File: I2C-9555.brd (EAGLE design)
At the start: 99.4 x 80.6 mm, 80 parts, among them IC1 PCA9555D, J1 I2CRA, J10 DCJ0202-RA, J2 I2CRA, J5 GROVE-4P-2.0-3470130P1, J8 GROVE-4P-2.0-3470130P1, Q0 MOSFET-P-044021001, Q1 MOSFET-P-044021001, Q10 MOSFET-P-044021001, Q11 MOSFET-P-044021001, Q12 MOSFET-P-044021001, Q13 MOSFET-P-044021001, Q14 MOSFET-P-044021001, Q15 MOSFET-P-044021001, Q2 MOSFET-P-044021001, Q3 MOSFET-P-044021001, Q4 MOSFET-P-044021001, Q5 MOSFET-P-044021001, Q6 MOSFET-P-044021001, Q7 MOSFET-P-044021001, Q8 MOSFET-P-044021001, Q9 MOSFET-P-044021001

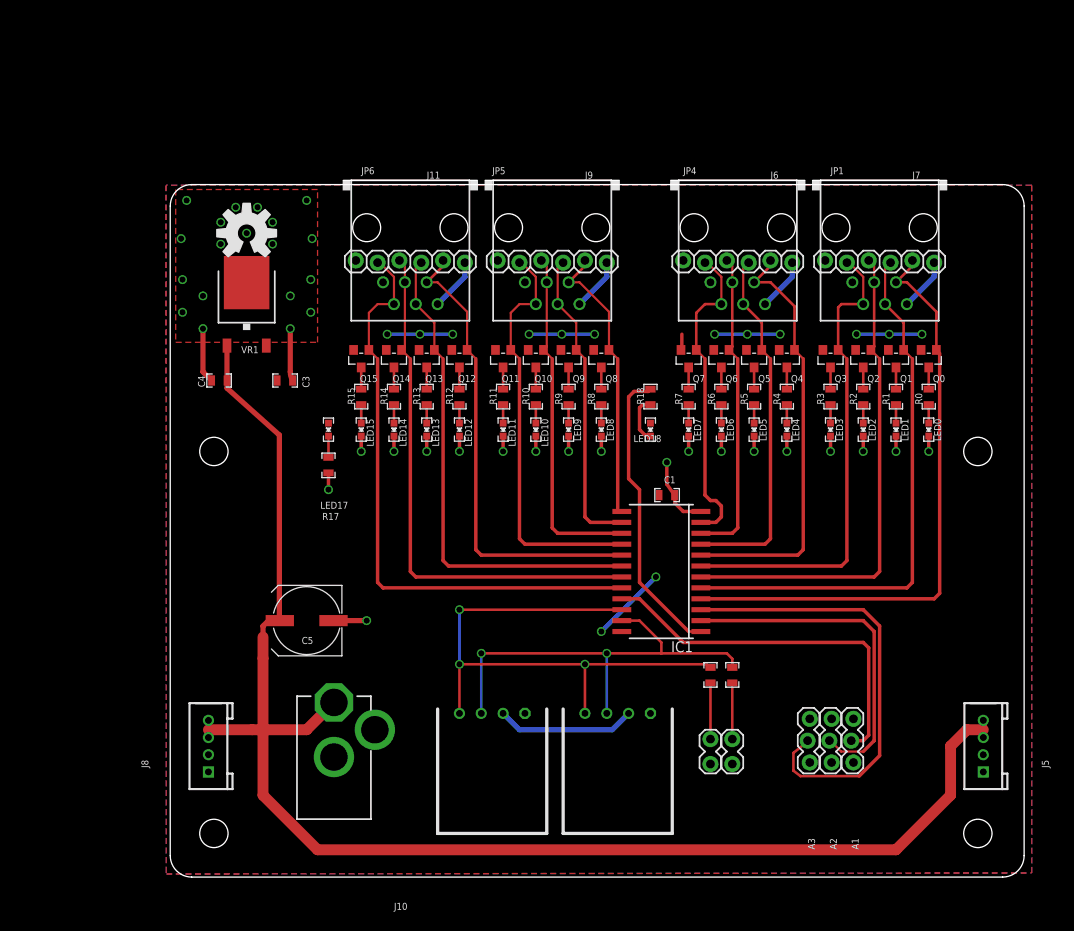
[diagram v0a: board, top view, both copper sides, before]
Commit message: new IOB and power connectors
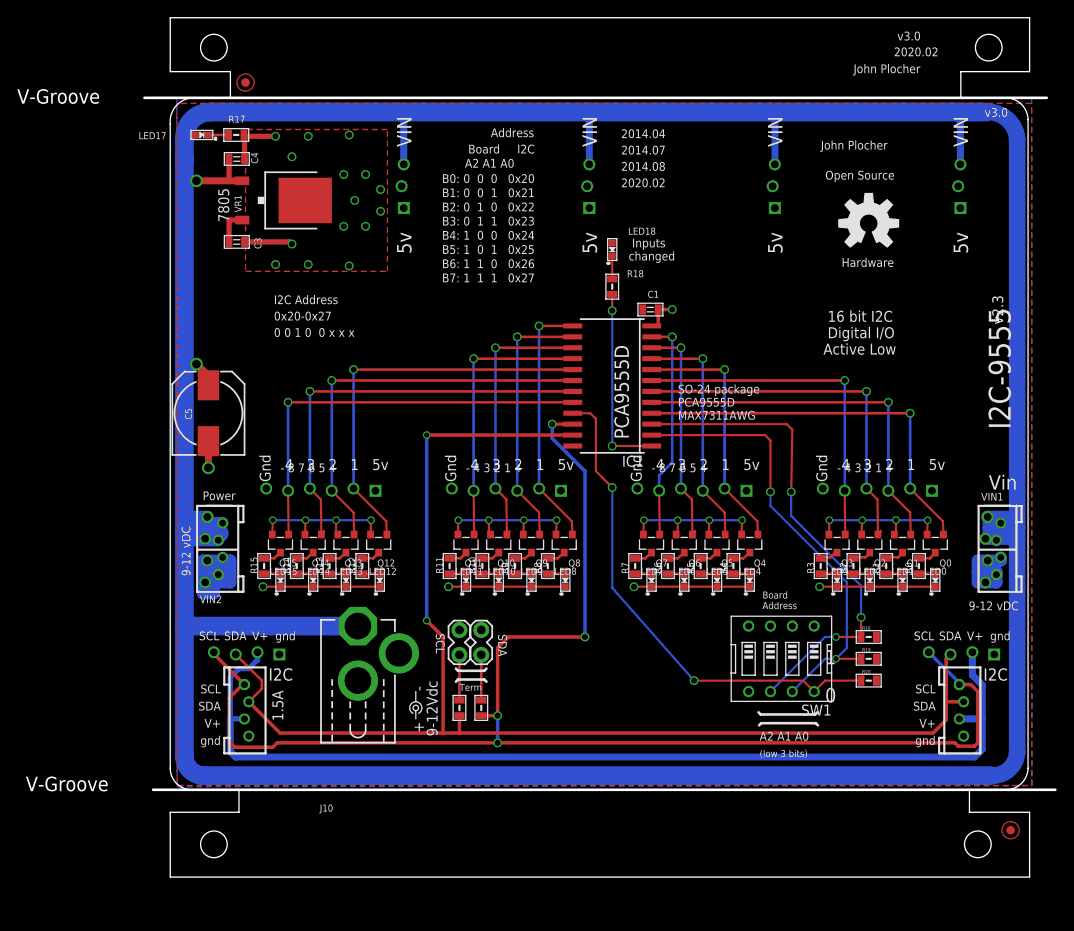
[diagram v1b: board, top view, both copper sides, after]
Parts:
- removed A1, A2, A3: (no value), SparkFun-Connectors:1X03_LOCK
- removed J11, J6, J7, J9: (no value), SPCoast:RJ11-NO_SHIELD
- removed J5, J8: GROVE-4P-2.0-3470130P1, OPL:4P-2.0
- removed JP1, JP4, JP5, JP6: (no value), SparkFun-Connectors:1X06_LOCK
- added BOARD1: BOARD80X100-IOB, SPCoast:BOARD-DINRAIL-3.17IN-IOB
- added FID1, FID2: FIDUCIAL, SPCoast:FIDUCIAL_1MM
- added R16, R19, R20: 10K, SPCoast:0805-RES
- added SW1: (no value), SPCoast:EDG-04
- added U$2, U$3, U$4, U$5: CONNECTOR-IO4-IOBBARE, SPCoast:IO4-IOB
- added VIN1: CONNECTOR-POWER-L, SPCoast:POWER-R2
- added VIN2: CONNECTOR-POWER-R, SPCoast:POWER-R
- C5: device rcl:UD-8X10_NICHICON -> SPCoast:0810-CAP
- J1, J2: value I2CRA -> (none); device SPCoast:I2C -> SPCoast:I2C-L
- J10: value DCJ0202-RA -> (none)
- LED17, LED18: value G - 0330010P1 -> G
- POWER: device SPCoast:POWER_USAGE -> SPCoast:PWR_LABEL
- Q0, Q1, Q10, Q11, Q12, Q13, Q14, Q15, Q2, Q3, Q4, Q5, Q6, Q7, Q8, Q9: value MOSFET-P-044021001 -> (none); device OPL:SOT23 -> SPCoast:SOT23-3
- moved U$1 72.4 mm to (81.3, 76.1)
- moved J1 40.6 mm to (92.1, 26.0)
- moved R17 39.9 mm to (7.68, 86.4), turned to 0 degrees
- moved LED17 37.3 mm to (3.68, 86.4), turned to 0 degrees
- moved SCL 33.3 mm to (33.7, 26.0), turned to 90 degrees
- moved R23 32.0 mm to (33.7, 19.7), turned to 270 degrees
- moved J2 29.4 mm to (8.89, 26.0)
- moved SDA 28.5 mm to (36.2, 26.0), turned to 90 degrees
- moved R22 26.9 mm to (36.2, 19.7), turned to 270 degrees
- moved C5 26.7 mm to (4.45, 54.0), turned to 90 degrees
- moved C4 25.9 mm to (7.75, 83.6), turned to 0 degrees
- moved Q12 23.4 mm to (24.3, 38.9)
- moved Q13 23.4 mm to (20.4, 38.9)
- moved Q14 23.4 mm to (16.6, 38.9)
- moved Q15 23.4 mm to (12.8, 38.9)
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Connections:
- net +9V: now also U$2.V+, U$3.V+, U$4.V+, U$5.V+, VIN1.V+, VIN1.V+@1, VIN1.V+@2, VIN1.V+@3, VIN2.V+, VIN2.V+@1, VIN2.V+@2, VIN2.V+@3; no longer J5.3, J5.4, J8.3, J8.4
- net A0: now also R20.1, SW1.8; no longer A1.2
- net A1: now also R19.1, SW1.7; no longer A2.2
- net A2: now also R16.1, SW1.6; no longer A3.2
- net GND: now also J1.GND@1, J2.GND@1, SW1.1, SW1.2, SW1.3, U$2.G@3, U$3.G@3, U$4.G@3, U$5.G@3, VIN1.GND, VIN1.GND@1, VIN1.GND@2, VIN1.GND@3, VIN2.GND, VIN2.GND@1, VIN2.GND@2, VIN2.GND@3; no longer A1.3, A2.3, A3.3, J11.6, J5.1, J5.2, J6.6, J7.6, J8.1, J8.2, J9.6, JP1.1, JP4.1, JP5.1, JP6.1
- net N$39: now also J1.V+@1, J2.V+@1
- net P1: now also U$2.P1; no longer J7.2, JP1.5
- net P10: now also U$4.P2; no longer J9.3, JP5.4
- net P11: now also U$4.P3; no longer J9.4, JP5.3
- net P12: now also U$4.P4; no longer J9.5, JP5.2
- net P13: now also U$5.P1; no longer J11.2, JP6.5
- net P14: now also U$5.P2; no longer J11.3, JP6.4
- net P15: now also U$5.P3; no longer J11.4, JP6.3
- net P16: now also U$5.P4; no longer J11.5, JP6.2
- net P2: now also U$2.P2; no longer J7.3, JP1.4
- net P3: now also U$2.P3; no longer J7.4, JP1.3
- net P4: now also U$2.P4; no longer J7.5, JP1.2
- net P5: now also U$3.P1; no longer J6.2, JP4.5
- net P6: now also U$3.P2; no longer J6.3, JP4.4
- net P7: now also U$3.P3; no longer J6.4, JP4.3
- net P8: now also U$3.P4; no longer J6.5, JP4.2
- net P9: now also U$4.P1; no longer J9.2, JP5.5
- net SCL: now also J1.SCL@1, J2.SCL@1
- net SDA: now also J1.SDA@1, J2.SDA@1
- net VCC: now also R16.2, R19.2, R20.2, U$2.V5, U$2.V5@1, U$3.V5, U$3.V5@1, U$4.V5, U$4.V5@1, U$5.V5, U$5.V5@1; no longer A1.1, A2.1, A3.1, J11.1, J6.1, J7.1, J9.1, JP1.6, JP4.6, JP5.6, JP6.6
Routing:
- net +9V: track 173.3 -> 439.1 mm, vias 0 -> 2
- net SDA: track 51.4 -> 155.0 mm
- net N$39: track 16.2 -> 117.8 mm
- net SCL: track 66.0 -> 166.7 mm, vias 3 -> 4
- net GND: track 55.4 -> 102.6 mm, vias 38 -> 21
- net P1: track 70.4 -> 45.8 mm, vias 0 -> 1
- net P16: track 69.6 -> 48.5 mm, vias 0 -> 1
- net P5: track 50.1 -> 29.3 mm, vias 0 -> 1
- net P2: track 63.7 -> 44.0 mm, vias 0 -> 1
- net P12: track 48.0 -> 32.0 mm, vias 0 -> 1
- net P4: track 56.0 -> 40.4 mm, vias 0 -> 1
- net P3: track 58.1 -> 42.7 mm, vias 0 -> 1
- net A0: track 43.6 -> 58.3 mm, vias 0 -> 2
- net P6: track 42.1 -> 27.5 mm, vias 0 -> 1
- net P15: track 61.9 -> 48.3 mm, vias 0 -> 1
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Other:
- board size 99.4 x 80.6 mm -> 106 x 100 mm
- board text added: "16 bit I2C Digital I/O Active Low"
- board text added: "2020.02"
- board text added: "A2 A1 A0"
- board text added: "SO-24 package PCA9555D MAX7311AWG"
- board text added: "v3.0"
- board text removed: ""Input Changed" LED fixed"
- board text removed: "16 bit I2C Digital I/O with feedback (4x IO4 ports)"
- board text removed: "A3 A3 A1"
- board text removed: "Active Low feedback LEDs"
- board text removed: "I2C-9555"
- board text removed: "IO4"
- board text removed: "changed to 3.18" form factor, added feedback LEDs"
